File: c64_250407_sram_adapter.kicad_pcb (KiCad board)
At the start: 2 copper layers, 53.3 x 59.7 mm, 19 parts, among them J1 TL_DRAM, J10 B_03, J2 TR_DRAM, J3 BL_DRAM, J4 BR_DRAM, J5 T_01, J6 T_02, J7 T_03, J8 B_01, J9 B_02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

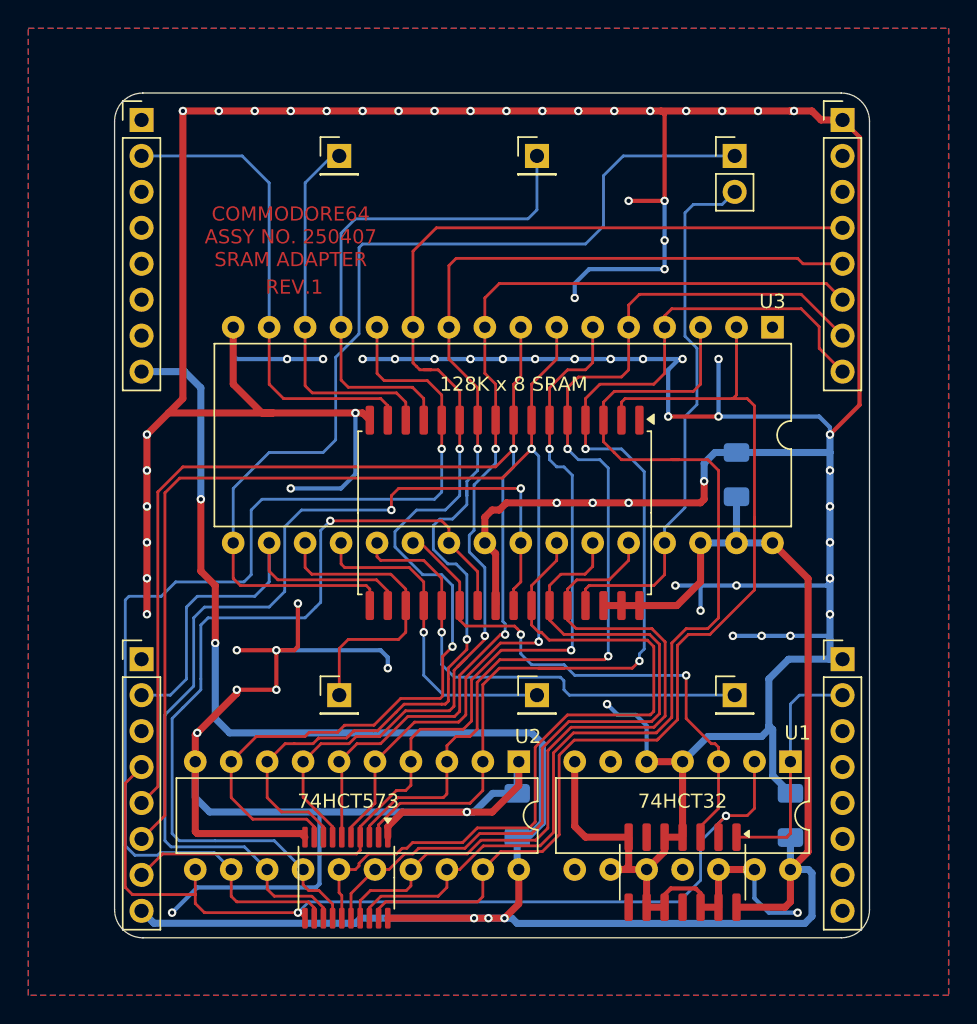
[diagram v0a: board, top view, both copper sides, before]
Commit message: Updated PCB to rev.2, adding optional /CAS delay cap
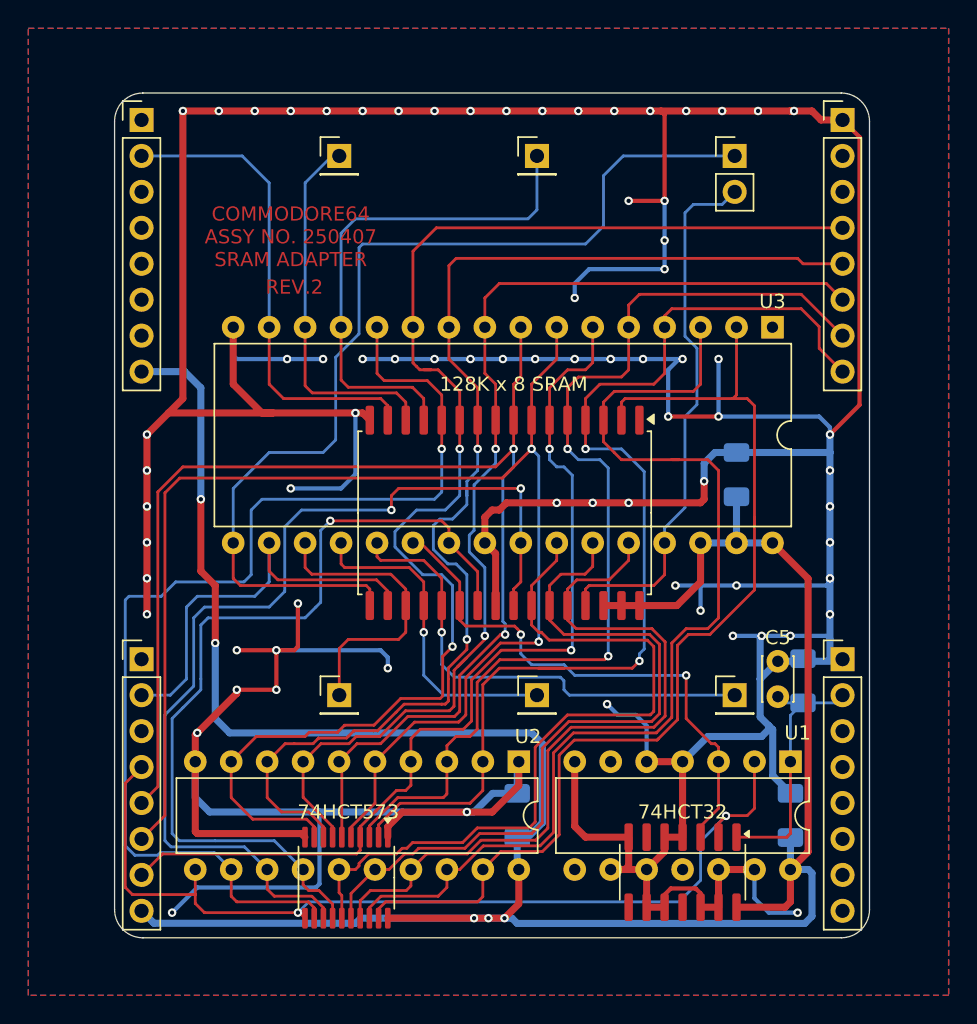
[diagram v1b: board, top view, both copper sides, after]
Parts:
- added C4: 100pF-820pF, Capacitor_SMD:C_1206_3216Metric_Pad1.33x1.80mm_HandSolder, B.Cu at (84.5, 78.4)
- added C5: 100pF-820pF, Capacitor_THT:C_Disc_D3.0mm_W2.0mm_P2.50mm, F.Cu at (82.7, 79.5)
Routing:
- net GND: track 454.9 -> 459.7 mm
- net /~{CAS}: track 17.0 -> 18.5 mm
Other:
- board text added: "If C204 on the motherboard is not fitted and the SRAM replacement is unstable, fit either C5 (THT) or C4 (SMD)."
- board text added: "REV.2"
- board text removed: "REV.1"

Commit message: Fixed the silkscreen
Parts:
- C4, C5: value 100pF-820pF -> 82pF-820pF
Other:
- board text added: "If C203 on the motherboard is not fitted and the SRAM replacement is unstable, fit either C5 (THT) or C4 (SMD)."
- board text removed: "If C204 on the motherboard is not fitted and the SRAM replacement is unstable, fit either C5 (THT) or C4 (SMD)."
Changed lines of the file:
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@@
 			)
 		)
-		(property "Value" "100pF-820pF"
+		(property "Value" "82pF-820pF"
 			(at 1.25 2.25 90)
 			(layer "F.Fab")
@@
 			)
 		)
-		(property "Value" "100pF-820pF"
+		(property "Value" "82pF-820pF"
 			(at 0 -1.85 90)
 			(layer "B.Fab")
@@
 		)
 	)
-	(gr_text "If C204 on the motherboard\nis not fitted and the SRAM\nreplacement is unstable, fit \neither C5 (THT) or C4 (SMD)."
-		(at 71.882 74.295 -0)
+	(gr_text "If C203 on the motherboard\nis not fitted and the SRAM\nreplacement is unstable, fit \neither C5 (THT) or C4 (SMD)."
+		(at 71.882 74.295 0)
 		(layer "B.SilkS")
 		(effects
